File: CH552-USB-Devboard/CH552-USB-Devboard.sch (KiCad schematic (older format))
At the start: 33 parts, among them J1 Conn_01x11_Male, J2 Conn_01x11_Male, J3 USB_C_Receptacle, SW1 SW_Push, SW2 SW_Push, U1 CH552T, U2 CH552G

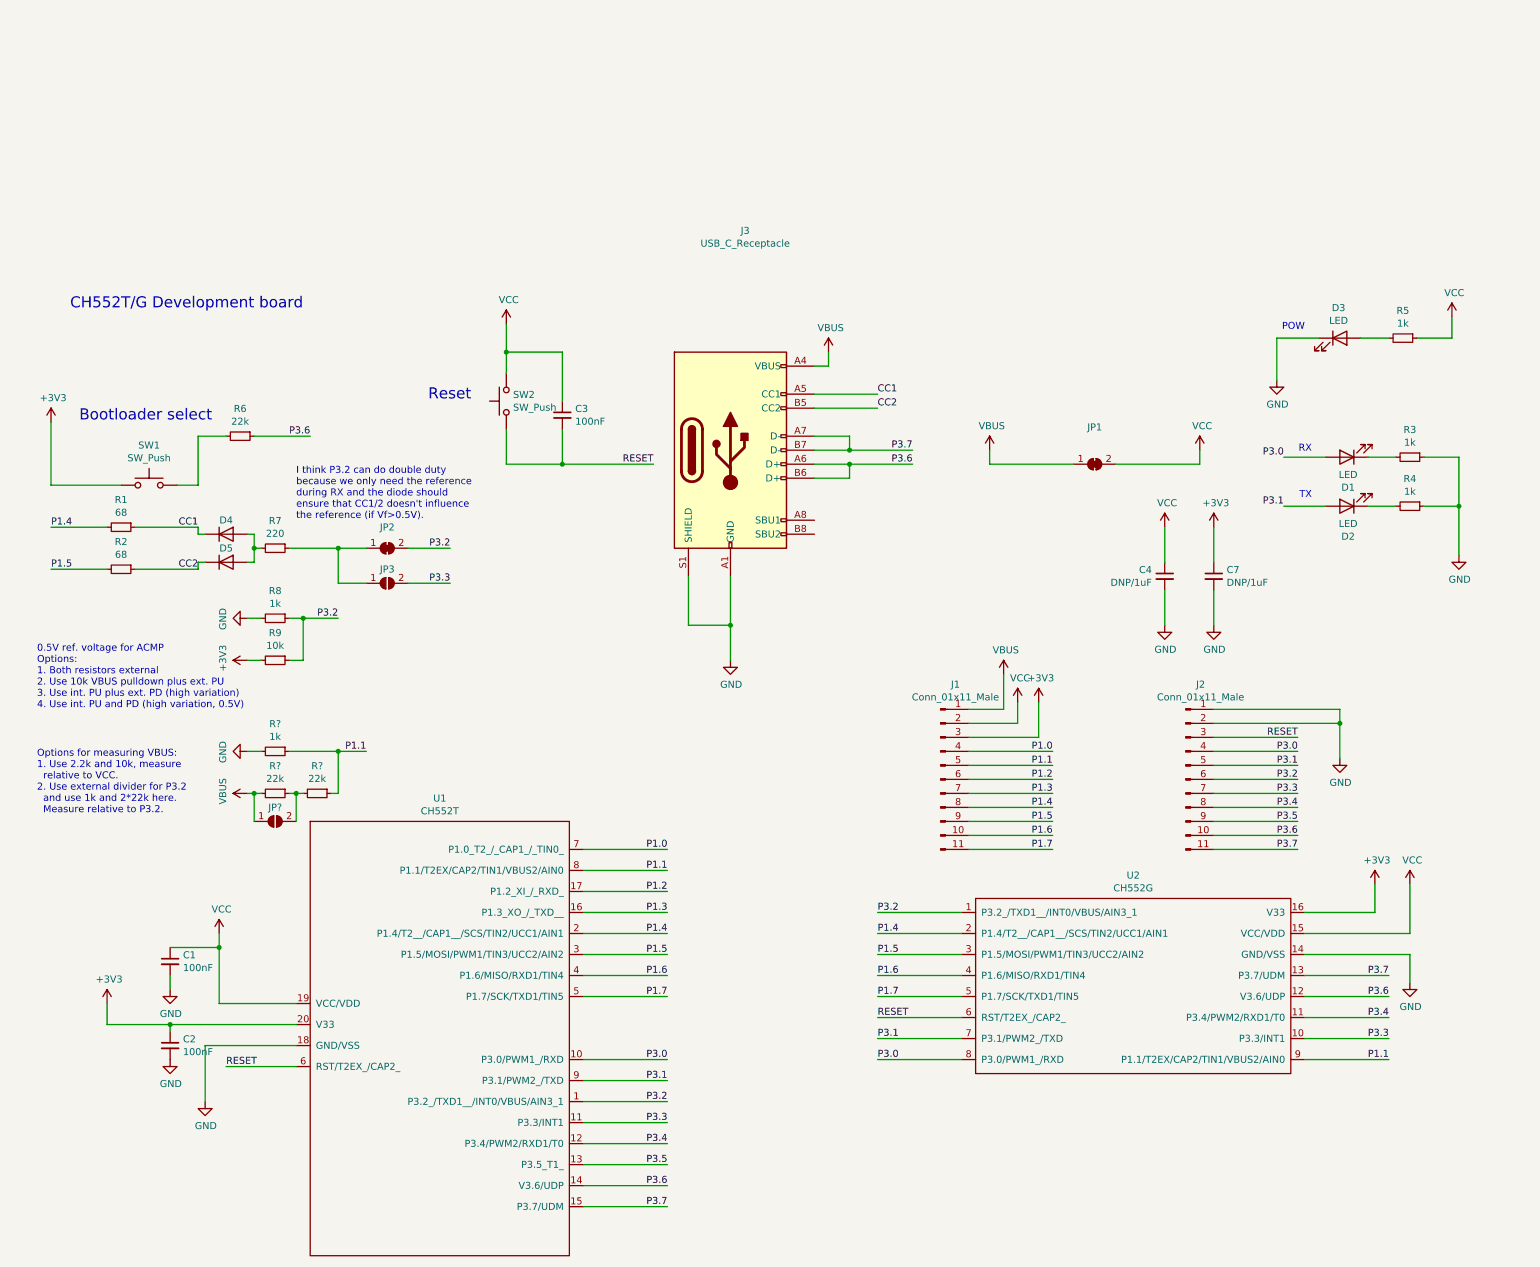
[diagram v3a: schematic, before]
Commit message: add 2nd USB connector, dedicated to PD monitoring
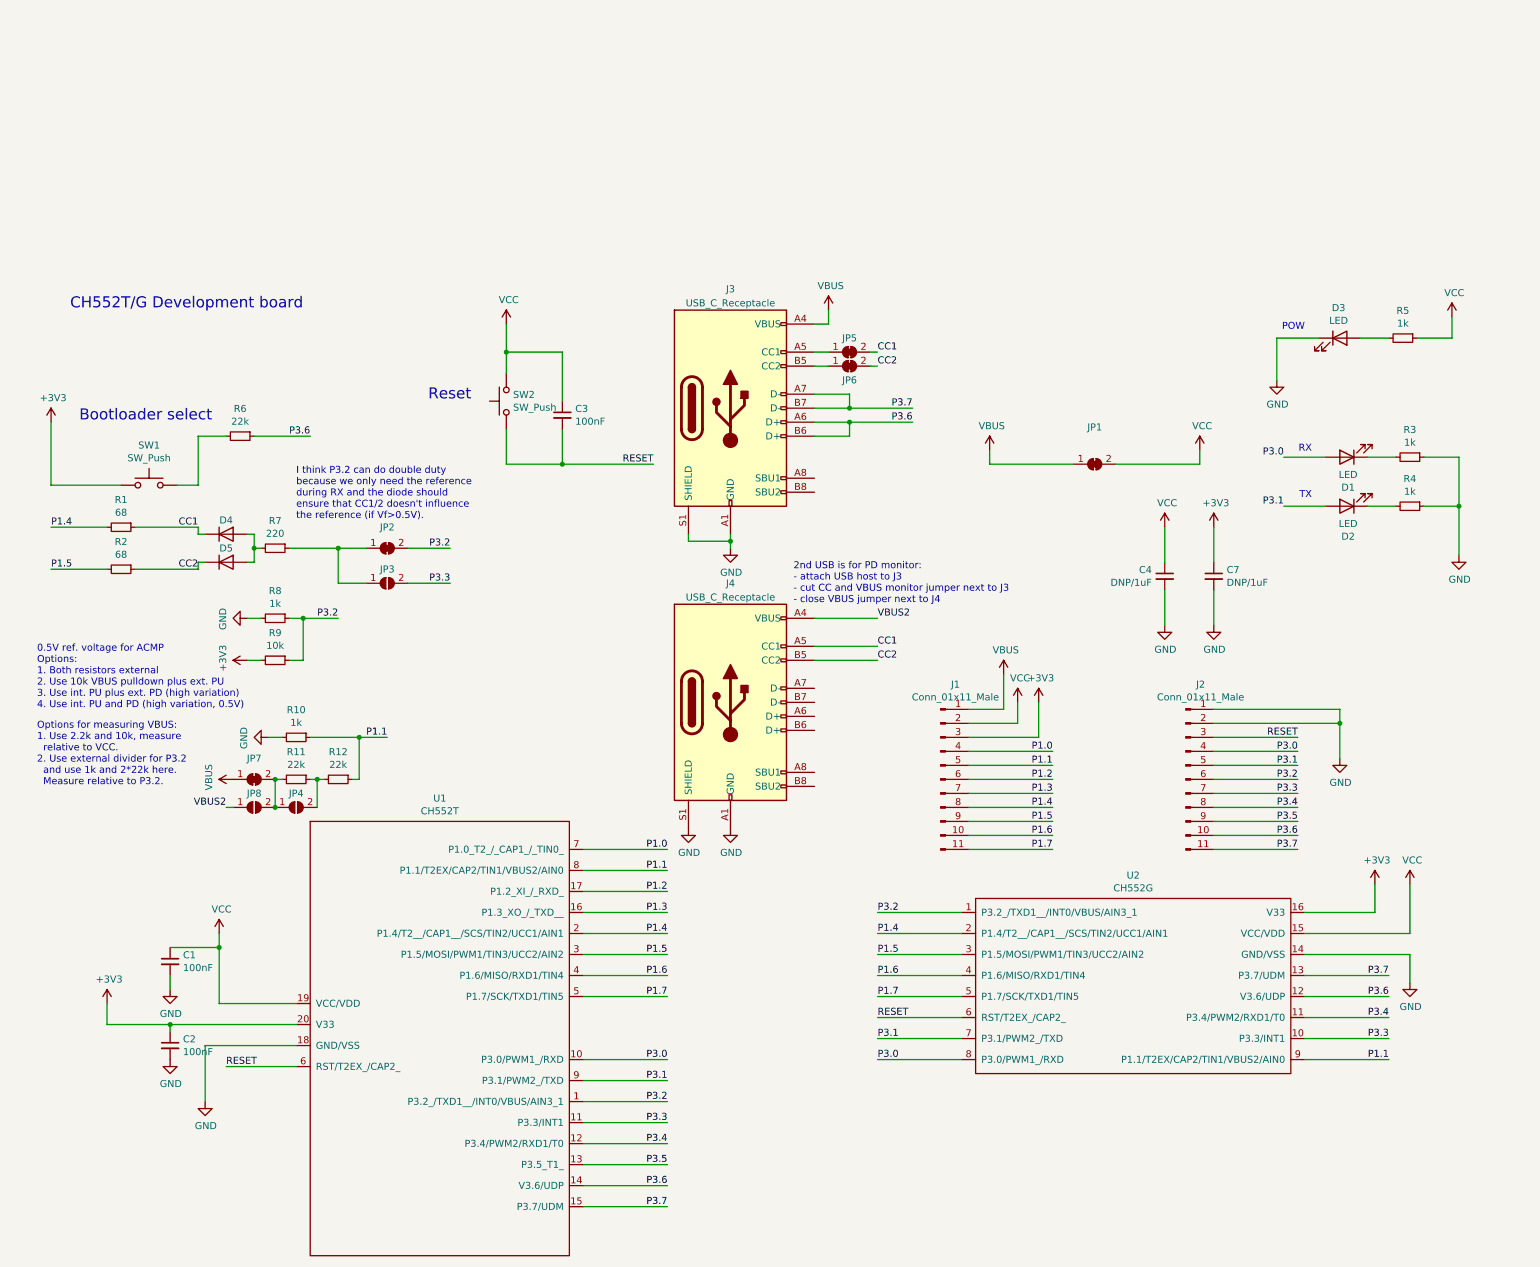
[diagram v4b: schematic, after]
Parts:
- added J4: USB_C_Receptacle, footprint:VACON_CSP_USC16_TR, symbol Connector:USB_C_Receptacle_USB2.0
- added JP5, JP6, JP7: Jumper, Jumper:SolderJumper-2_P1.3mm_Bridged_RoundedPad1.0x1.5mm, symbol Jumper:SolderJumper_2_Bridged
- added JP8: Jumper, Jumper:SolderJumper-2_P1.3mm_Open_RoundedPad1.0x1.5mm, symbol Jumper:SolderJumper_2_Open
- gave numbers to parts that had none: 4
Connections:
- net CC1: now also J4.A5 (CC1), JP5.2 (B); no longer J3.A5 (CC1)
- net CC2: now also J4.B5 (CC2), JP6.2 (B); no longer J3.B5 (CC2)
- net GND: now also J4.A1 (GND), J4.A12 (GND), J4.B1 (GND), J4.B12 (GND), J4.S1 (SHIELD)
- net VBUS: now also JP7.1 (A); no longer JP4.1 (A), R11.2
- new net: J3.A5 (CC1), JP5.1 (A)
- new net: J3.B5 (CC2), JP6.1 (A)
- new net: JP4.1 (A), JP7.2 (B), JP8.2 (B), R11.2
- new net VBUS2: J4.A4 (VBUS), J4.A9 (VBUS), J4.B4 (VBUS), J4.B9 (VBUS), JP8.1 (A)
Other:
- note added: "2nd USB is for PD monitor:\n- attach USB host to J3\n- cut CC and VBUS monitor jumper next to J3\n- close VBUS jumper next to J4"
- moved on the sheet: J3, JP4, R10, R11, R12
